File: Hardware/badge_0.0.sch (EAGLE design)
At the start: 43 parts, among them CON1 PH_2, IC1 CP2102, J3 2X6 FEMALE, SW1 MK12C02, SW2 MK12C02, U4 MCP73832T-2DCI/OT

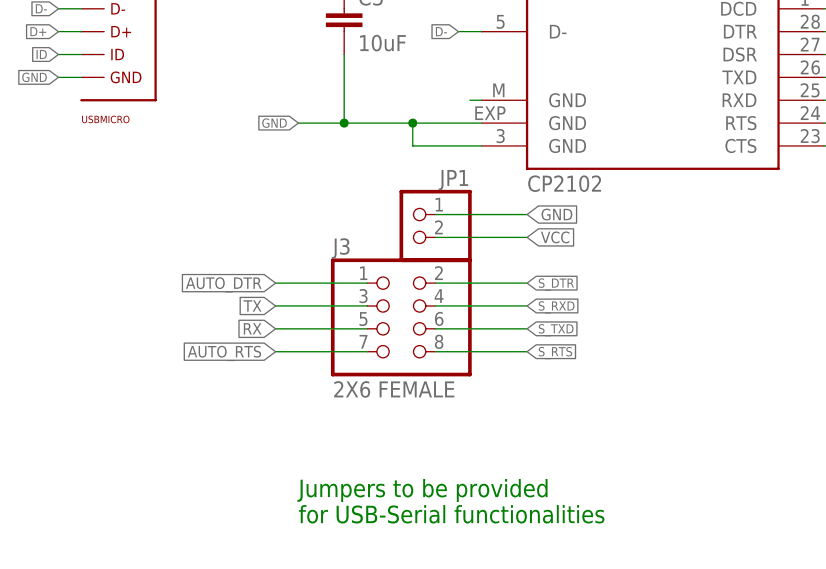
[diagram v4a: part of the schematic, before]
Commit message: Swapped a silks, added more silks, bit of routing changes
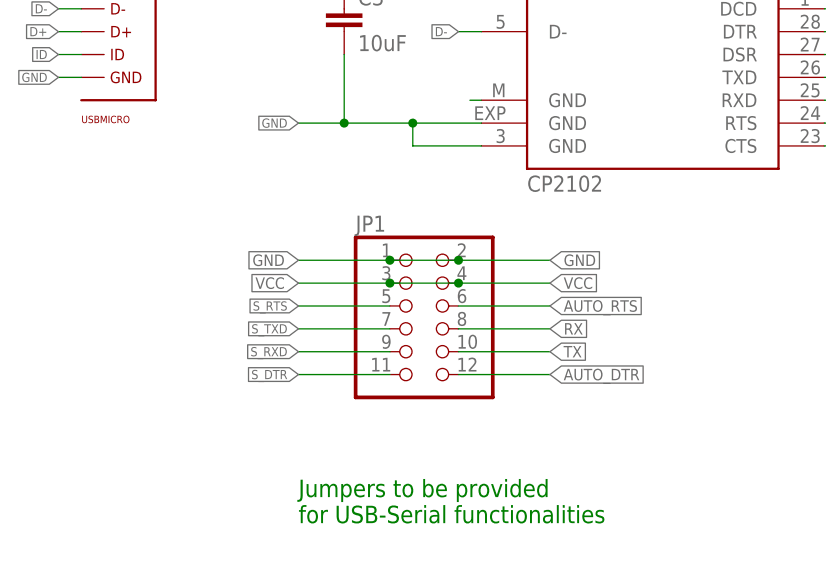
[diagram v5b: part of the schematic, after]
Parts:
- removed J3: 2X6 FEMALE, adafruit:PINHD-2X4
- JP1: device pinhead:PINHD-1X2 -> pinhead:PINHD-2X6
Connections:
- net AUTO_DTR: now also JP1.12; no longer J3.1
- net AUTO_RTS: now also JP1.6; no longer J3.7
- net GND: now also JP1.2
- net RX: now also JP1.8; no longer J3.5
- net S_DTR: now also JP1.11; no longer J3.2
- net S_RTS: now also JP1.5; no longer J3.8
- net S_RXD: now also JP1.9; no longer J3.4
- net S_TXD: now also JP1.7; no longer J3.6
- net TX: now also JP1.10; no longer J3.3
- net VCC: now also JP1.3, JP1.4; no longer JP1.2
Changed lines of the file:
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@@
 <setting verticaltext="up"/>
 </settings>
-<grid distance="0.05" unitdist="inch" unit="inch" style="lines" multiple="1" display="yes" altdistance="0.05" altunitdist="inch" altunit="inch"/>
+<grid distance="0.1" unitdist="inch" unit="inch" style="lines" multiple="1" display="no" altdistance="0.01" altunitdist="inch" altunit="inch"/>
 <layers>
 <layer number="1" name="Top" color="4" fill="1" visible="no" active="no"/>
@@
 <part name="CON1" library="badge" deviceset="PH_2" device=""/>
 <part name="IC1" library="silabs" deviceset="CP210*" device="" technology="2"/>
-<part name="J3" library="adafruit" deviceset="PINHD-2X4" device="" value="2X6 FEMALE"/>
 <part name="J2" library="SparkFun-Connectors" deviceset="M08" device="SILK_FEMALE_PTH"/>
 <part name="J1" library="SparkFun-Connectors" deviceset="M03" device="PTH"/>
@@
 <part name="U$13" library="LYS_special" deviceset="PEMH9,115" device=""/>
 <part name="SJ1" library="jumper" deviceset="SJ" device=""/>
-<part name="JP1" library="pinhead" deviceset="PINHD-1X2" device=""/>
+<part name="JP1" library="pinhead" deviceset="PINHD-2X6" device=""/>
 </parts>
 <sheets>
@@
 <instance part="CON1" gate="G$1" x="224.79" y="214.63" rot="MR0"/>
 <instance part="IC1" gate="G$1" x="81.28" y="213.36"/>
-<instance part="J3" gate="A" x="53.34" y="177.8"/>
 <instance part="J2" gate="G$1" x="132.08" y="208.28" rot="R180"/>
 <instance part="J1" gate="J$1" x="134.62" y="226.06" rot="R180"/>
@@
 <instance part="U$13" gate="G$1" x="154.94" y="123.19"/>
 <instance part="SJ1" gate="1" x="143.51" y="41.91"/>
-<instance part="JP1" gate="G$1" x="55.88" y="187.96" rot="MR0"/>
+<instance part="JP1" gate="A" x="55.88" y="180.34"/>
 </instances>
 <busses>
@@
 </segment>
 <segment>
-<pinref part="JP1" gate="G$1" pin="2"/>
-<wire x1="58.42" y1="187.96" x2="68.58" y2="187.96" width="0.1524" layer="91"/>
-<label x="68.58" y="187.96" size="1.27" layer="95" xref="yes"/>
+<wire x1="60.96" y1="182.88" x2="71.12" y2="182.88" width="0.1524" layer="91"/>
+<label x="71.12" y="182.88" size="1.27" layer="95" xref="yes"/>
+<pinref part="JP1" gate="A" pin="4"/>
+<pinref part="JP1" gate="A" pin="3"/>
+<wire x1="53.34" y1="182.88" x2="60.96" y2="182.88" width="0.1524" layer="91"/>
+<junction x="60.96" y="182.88"/>
+<wire x1="53.34" y1="182.88" x2="43.18" y2="182.88" width="0.1524" layer="91"/>
+<junction x="53.34" y="182.88"/>
+<label x="43.18" y="182.88" size="1.27" layer="95" rot="R180" xref="yes"/>
 </segment>
 </net>
@@
 </segment>
 <segment>
-<pinref part="JP1" gate="G$1" pin="1"/>
-<wire x1="58.42" y1="190.5" x2="68.58" y2="190.5" width="0.1524" layer="91"/>
-<label x="68.58" y="190.5" size="1.27" layer="95" xref="yes"/>
+<wire x1="60.96" y1="185.42" x2="71.12" y2="185.42" width="0.1524" layer="91"/>
+<label x="71.12" y="185.42" size="1.27" layer="95" xref="yes"/>
+<pinref part="JP1" gate="A" pin="2"/>
+<pinref part="JP1" gate="A" pin="1"/>
+<wire x1="60.96" y1="185.42" x2="53.34" y2="185.42" width="0.1524" layer="91"/>
+<junction x="60.96" y="185.42"/>
+<wire x1="53.34" y1="185.42" x2="43.18" y2="185.42" width="0.1524" layer="91"/>
+<junction x="53.34" y="185.42"/>
+<label x="43.18" y="185.42" size="1.27" layer="95" rot="R180" xref="yes"/>
 </segment>
 </net>
@@
 </segment>
 <segment>
-<label x="40.64" y="180.34" size="1.27" layer="95" rot="R180" xref="yes"/>
-<wire x1="40.64" y1="180.34" x2="50.8" y2="180.34" width="0.1524" layer="91"/>
-<pinref part="J3" gate="A" pin="3"/>
+<label x="71.12" y="175.26" size="1.27" layer="95" xref="yes"/>
+<wire x1="71.12" y1="175.26" x2="60.96" y2="175.26" width="0.1524" layer="91"/>
+<pinref part="JP1" gate="A" pin="10"/>
 </segment>
 <segment>
@@
 </segment>
 <segment>
-<label x="40.64" y="177.8" size="1.27" layer="95" rot="R180" xref="yes"/>
-<wire x1="50.8" y1="177.8" x2="40.64" y2="177.8" width="0.1524" layer="91"/>
-<pinref part="J3" gate="A" pin="5"/>
+<label x="71.12" y="177.8" size="1.27" layer="95" xref="yes"/>
+<wire x1="60.96" y1="177.8" x2="71.12" y2="177.8" width="0.1524" layer="91"/>
+<pinref part="JP1" gate="A" pin="8"/>
 </segment>
 <segment>
@@
 </segment>
 <segment>
-<pinref part="J3" gate="A" pin="2"/>
-<wire x1="68.58" y1="182.88" x2="58.42" y2="182.88" width="0.1524" layer="91"/>
-<label x="68.58" y="182.88" size="1.016" layer="95" xref="yes"/>
+<wire x1="43.18" y1="172.72" x2="53.34" y2="172.72" width="0.1524" layer="91"/>
+<label x="43.18" y="172.72" size="1.016" layer="95" rot="R180" xref="yes"/>
+<pinref part="JP1" gate="A" pin="11"/>
 </segment>
 </net>
@@
 </segment>
 <segment>
-<pinref part="J3" gate="A" pin="6"/>
-<wire x1="68.58" y1="177.8" x2="58.42" y2="177.8" width="0.1524" layer="91"/>
-<label x="68.58" y="177.8" size="1.016" layer="95" xref="yes"/>
+<wire x1="43.18" y1="177.8" x2="53.34" y2="177.8" width="0.1524" layer="91"/>
+<label x="43.18" y="177.8" size="1.016" layer="95" rot="R180" xref="yes"/>
+<pinref part="JP1" gate="A" pin="7"/>
 </segment>
 </net>
@@
 </segment>
 <segment>
-<pinref part="J3" gate="A" pin="4"/>
-<wire x1="68.58" y1="180.34" x2="58.42" y2="180.34" width="0.1524" layer="91"/>
-<label x="68.58" y="180.34" size="1.016" layer="95" xref="yes"/>
+<wire x1="43.18" y1="175.26" x2="53.34" y2="175.26" width="0.1524" layer="91"/>
+<label x="43.18" y="175.26" size="1.016" layer="95" rot="R180" xref="yes"/>
+<pinref part="JP1" gate="A" pin="9"/>
 </segment>
 </net>
@@
 </segment>
 <segment>
-<label x="68.58" y="175.26" size="1.016" layer="95" xref="yes"/>
-<pinref part="J3" gate="A" pin="8"/>
-<wire x1="58.42" y1="175.26" x2="68.58" y2="175.26" width="0.1524" layer="91"/>
+<label x="43.18" y="180.34" size="1.016" layer="95" rot="R180" xref="yes"/>
+<wire x1="53.34" y1="180.34" x2="43.18" y2="180.34" width="0.1524" layer="91"/>
+<pinref part="JP1" gate="A" pin="5"/>
 </segment>
 </net>
@@
 <net name="AUTO_DTR" class="0">
 <segment>
-<pinref part="J3" gate="A" pin="1"/>
-<wire x1="50.8" y1="182.88" x2="40.64" y2="182.88" width="0.1524" layer="91"/>
-<label x="40.64" y="182.88" size="1.27" layer="95" rot="R180" xref="yes"/>
+<wire x1="60.96" y1="172.72" x2="71.12" y2="172.72" width="0.1524" layer="91"/>
+<label x="71.12" y="172.72" size="1.27" layer="95" xref="yes"/>
+<pinref part="JP1" gate="A" pin="12"/>
 </segment>
 <segment>
@@
 <net name="AUTO_RTS" class="0">
 <segment>
-<label x="40.64" y="175.26" size="1.27" layer="95" rot="R180" xref="yes"/>
-<pinref part="J3" gate="A" pin="7"/>
-<wire x1="40.64" y1="175.26" x2="50.8" y2="175.26" width="0.1524" layer="91"/>
-</segment>
-<segment>
+<label x="71.12" y="180.34" size="1.27" layer="95" xref="yes"/>
+<wire x1="71.12" y1="180.34" x2="60.96" y2="180.34" width="0.1524" layer="91"/>
+<pinref part="JP1" gate="A" pin="6"/>
+</segment>
+<segment>

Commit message: added some changes from YS
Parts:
- added SJ2: SOLDERJUMPERTRACE, SparkFun-Retired:SOLDERJUMPERTRACE
- SJ1: value (none) -> SOLDERJUMPERTRACE; device jumper:SJ -> SparkFun-Retired:SOLDERJUMPERTRACE
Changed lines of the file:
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@@
 <?xml version="1.0" encoding="utf-8"?>
 <!DOCTYPE eagle SYSTEM "eagle.dtd">
-<eagle version="7.1.0">
+<eagle version="7.5.0">
 <drawing>
 <settings>
@@
 <part name="FRAME1" library="frames" deviceset="A3L-LOC" device=""/>
 <part name="U$13" library="LYS_special" deviceset="PEMH9,115" device=""/>
-<part name="SJ1" library="jumper" deviceset="SJ" device=""/>
+<part name="SJ1" library="SparkFun-Retired" deviceset="SOLDERJUMPER" device="TRACE"/>
 <part name="JP1" library="pinhead" deviceset="PINHD-2X6" device=""/>
+<part name="SJ2" library="SparkFun-Retired" deviceset="SOLDERJUMPER" device="TRACE"/>
 </parts>
 <sheets>
@@
 <instance part="SJ1" gate="1" x="143.51" y="41.91"/>
 <instance part="JP1" gate="A" x="55.88" y="180.34"/>
+<instance part="SJ2" gate="1" x="142.24" y="33.02"/>
 </instances>
 <busses>

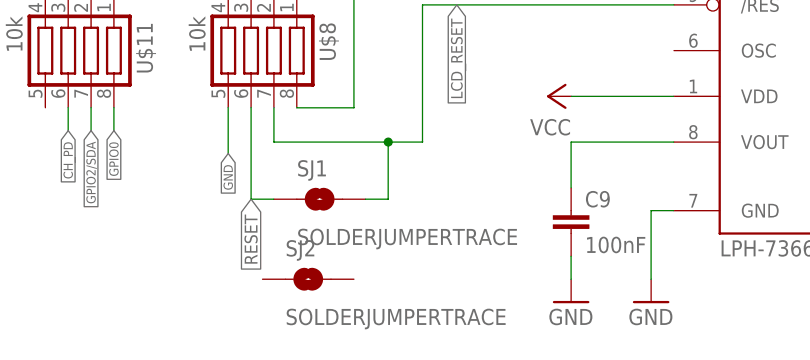
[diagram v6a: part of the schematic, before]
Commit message: deleted lone component
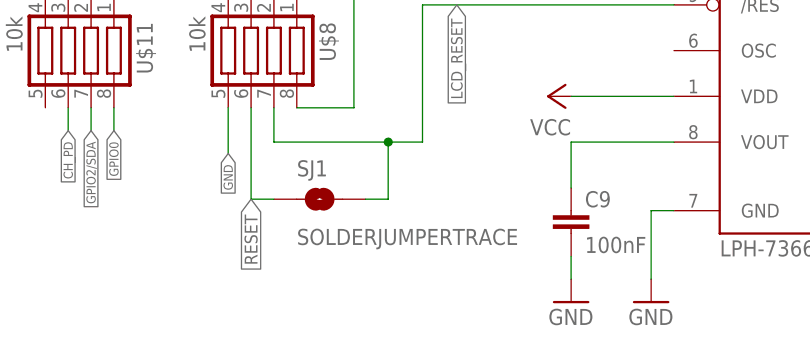
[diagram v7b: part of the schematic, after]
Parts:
- removed SJ2: SOLDERJUMPERTRACE, SparkFun-Retired:SOLDERJUMPERTRACE
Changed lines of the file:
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@@
 <part name="SJ1" library="SparkFun-Retired" deviceset="SOLDERJUMPER" device="TRACE"/>
 <part name="JP1" library="pinhead" deviceset="PINHD-2X6" device=""/>
-<part name="SJ2" library="SparkFun-Retired" deviceset="SOLDERJUMPER" device="TRACE"/>
 </parts>
 <sheets>
@@
 <instance part="SJ1" gate="1" x="143.51" y="41.91"/>
 <instance part="JP1" gate="A" x="55.88" y="180.34"/>
-<instance part="SJ2" gate="1" x="142.24" y="33.02"/>
 </instances>
 <busses>

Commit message: Minimal nonessential changes
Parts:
- SJ1: value SOLDERJUMPERTRACE -> LCD_RESET
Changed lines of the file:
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@@
 <?xml version="1.0" encoding="utf-8"?>
 <!DOCTYPE eagle SYSTEM "eagle.dtd">
-<eagle version="7.5.0">
+<eagle version="7.1.0">
 <drawing>
 <settings>
@@
 <part name="FRAME1" library="frames" deviceset="A3L-LOC" device=""/>
 <part name="U$13" library="LYS_special" deviceset="PEMH9,115" device=""/>
-<part name="SJ1" library="SparkFun-Retired" deviceset="SOLDERJUMPER" device="TRACE"/>
+<part name="SJ1" library="SparkFun-Retired" deviceset="SOLDERJUMPER" device="TRACE" value="LCD_RESET"/>
 <part name="JP1" library="pinhead" deviceset="PINHD-2X6" device=""/>
 </parts>
